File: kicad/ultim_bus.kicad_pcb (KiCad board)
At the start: 2 copper layers, 16 parts, among them P1 CONN_1, P10 CONN_1, P11 CONN_1, P12 CONN_1, P2 CONN_1, P3 CONN_1, P4 CONN_1, P5 CONN_1, P6 CONN_1, P7 CONN_1, P8 CONN_1, P9 CONN_1

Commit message: UlTiM8x8 board layout complete, Gerbers ready for fab
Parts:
- removed G***: LOGO, ultim8x8_libs:logo_ultim8x8_small
- removed G***: LOGO, ultim8x8_libs:logo_wyo_butterfly_small
- removed G***: LOGO, ultim8x8_libs:logo_MLlabs_small
- removed L101: OSHW, ultim8x8_libs:OSHW_6mm
- added L1: OSHW, ultim8x8_libs:OSHW_6mm, F.Cu at (210.8, 38.1)
- added L10: Maniacal, ultim8x8_libs:logo_MLlabs_small, F.Cu at (165.1, 55.9)
- added L11: Maniacal, ultim8x8_libs:logo_MLlabs_small, F.Cu at (149.9, 68.6)
- added L12: Maniacal, ultim8x8_libs:logo_MLlabs_small, F.Cu at (149.9, 91.4)
- added L13: ULTiM, ultim8x8_libs:logo_ultim8x8_small, F.Cu at (58.4, 38.1)
- added L14: ULTiM, ultim8x8_libs:logo_ultim8x8_small, F.Cu at (73.7, 55.9)
- added L15: ULTiM, ultim8x8_libs:logo_ultim8x8_small, F.Cu at (58.4, 69.2)
- added L16: ULTiM, ultim8x8_libs:logo_ultim8x8_small, F.Cu at (58.4, 91.4)
- added L2: OSHW, ultim8x8_libs:OSHW_6mm, F.Cu at (196.8, 55.2)
- added L3: OSHW, ultim8x8_libs:OSHW_6mm, F.Cu at (210.8, 68.6)
- added L4: OSHW, ultim8x8_libs:OSHW_6mm, F.Cu at (210.8, 91.4)
- added L5: WyoLum, ultim8x8_libs:logo_wyo_butterfly_small, F.Cu at (119.4, 38.1)
- added L6: WyoLum, ultim8x8_libs:logo_wyo_butterfly_small, F.Cu at (104.8, 57.1)
- added L7: WyoLum, ultim8x8_libs:logo_wyo_butterfly_small, F.Cu at (119.4, 68.6)
- added L8: WyoLum, ultim8x8_libs:logo_wyo_butterfly_small, F.Cu at (104.8, 92.1)
- added L9: Maniacal, ultim8x8_libs:logo_MLlabs_small, F.Cu at (149.9, 38.1)
- added P13: CONN_1, ultim8x8_libs:Screw, F.Cu at (50.8, 50.8)
- added P14: CONN_1, ultim8x8_libs:Screw, F.Cu at (66.0, 50.8)
- added P15: CONN_1, ultim8x8_libs:Screw, F.Cu at (81.3, 50.8)
- added P16: CONN_1, ultim8x8_libs:Screw, F.Cu at (96.5, 50.8)
- added P17: CONN_1, ultim8x8_libs:Screw, F.Cu at (111.8, 50.8)
- added P18: CONN_1, ultim8x8_libs:Screw, F.Cu at (127.0, 50.8)
- added P19: CONN_1, ultim8x8_libs:Screw, F.Cu at (142.2, 50.8)
- added P20: CONN_1, ultim8x8_libs:Screw, F.Cu at (157.5, 50.8)
- added P21: CONN_1, ultim8x8_libs:Screw, F.Cu at (172.7, 50.8)
- added P22: CONN_1, ultim8x8_libs:Screw, F.Cu at (188.0, 50.8)
- added P23: CONN_1, ultim8x8_libs:Screw, F.Cu at (203.2, 50.8)
- added P24: CONN_1, ultim8x8_libs:Screw, F.Cu at (218.4, 50.8)
- added P25: CONN_1, ultim8x8_libs:Screw, F.Cu at (58.4, 55.9)
- added P26: CONN_1, ultim8x8_libs:Screw, F.Cu at (88.9, 55.9)
- added P27: CONN_1, ultim8x8_libs:Screw, F.Cu at (119.4, 55.9)
- added P28: CONN_1, ultim8x8_libs:Screw, F.Cu at (149.9, 55.9)
- added P29: CONN_1, ultim8x8_libs:Screw, F.Cu at (180.3, 55.9)
- added P30: CONN_1, ultim8x8_libs:Screw, F.Cu at (210.8, 55.9)
- added P31: CONN_1, ultim8x8_libs:Screw, F.Cu at (50.8, 68.6)
- added P32: CONN_1, ultim8x8_libs:Screw, F.Cu at (66.0, 68.6)
- added P33: CONN_1, ultim8x8_libs:Screw, F.Cu at (81.3, 68.6)
- added P34: CONN_1, ultim8x8_libs:Screw, F.Cu at (96.5, 68.6)
- added P35: CONN_1, ultim8x8_libs:Screw, F.Cu at (111.8, 68.6)
- added P36: CONN_1, ultim8x8_libs:Screw, F.Cu at (127.0, 68.6)
- added P37: CONN_1, ultim8x8_libs:Screw, F.Cu at (142.2, 68.6)
- added P38: CONN_1, ultim8x8_libs:Screw, F.Cu at (157.5, 68.6)
- added P39: CONN_1, ultim8x8_libs:Screw, F.Cu at (172.7, 68.6)
- added P40: CONN_1, ultim8x8_libs:Screw, F.Cu at (188.0, 68.6)
- added P41: CONN_1, ultim8x8_libs:Screw, F.Cu at (203.2, 68.6)
- added P42: CONN_1, ultim8x8_libs:Screw, F.Cu at (218.4, 68.6)
- added P43: CONN_1, ultim8x8_libs:Screw, F.Cu at (50.8, 78.7)
- added P44: CONN_1, ultim8x8_libs:Screw, F.Cu at (81.3, 78.7)
- added P45: CONN_1, ultim8x8_libs:Screw, F.Cu at (111.8, 78.7)
- added P46: CONN_1, ultim8x8_libs:Screw, F.Cu at (142.2, 78.7)
- added P47: CONN_1, ultim8x8_libs:Screw, F.Cu at (172.7, 78.7)
- added P48: CONN_1, ultim8x8_libs:Screw, F.Cu at (203.2, 78.7)
- added P49: CONN_1, ultim8x8_libs:Screw, F.Cu at (50.8, 91.4)
- added P50: CONN_1, ultim8x8_libs:Screw, F.Cu at (66.0, 91.4)
- added P51: CONN_1, ultim8x8_libs:Screw, F.Cu at (81.3, 91.4)
- added P52: CONN_1, ultim8x8_libs:Screw, F.Cu at (96.5, 91.4)
- added P53: CONN_1, ultim8x8_libs:Screw, F.Cu at (111.8, 91.4)
- added P54: CONN_1, ultim8x8_libs:Screw, F.Cu at (127.0, 91.4)
- added P55: CONN_1, ultim8x8_libs:Screw, F.Cu at (142.2, 91.4)
- added P56: CONN_1, ultim8x8_libs:Screw, F.Cu at (157.5, 91.4)
- added P57: CONN_1, ultim8x8_libs:Screw, F.Cu at (172.7, 91.4)
- added P58: CONN_1, ultim8x8_libs:Screw, F.Cu at (188.0, 91.4)
- added P59: CONN_1, ultim8x8_libs:Screw, F.Cu at (203.2, 91.4)
- added P60: CONN_1, ultim8x8_libs:Screw, F.Cu at (218.4, 91.4)
- added P61: CONN_1, ultim8x8_libs:Screw, F.Cu at (66.0, 81.3)
- added P62: CONN_1, ultim8x8_libs:Screw, F.Cu at (96.5, 81.3)
- added P63: CONN_1, ultim8x8_libs:Screw, F.Cu at (127.0, 81.3)
- added P64: CONN_1, ultim8x8_libs:Screw, F.Cu at (157.5, 81.3)
- added P65: CONN_1, ultim8x8_libs:Screw, F.Cu at (188.0, 81.3)
- added P66: CONN_1, ultim8x8_libs:Screw, F.Cu at (218.4, 81.3)
- added mouse-bite-2.54mm-slot: VAL**, ultim8x8_libs:mouse-bite-2.54mm-slot, F.Cu at (96.5, 44.5)
- added mouse-bite-2.54mm-slot: VAL**, ultim8x8_libs:mouse-bite-2.54mm-slot, F.Cu at (127.0, 76.2)
- added mouse-bite-2.54mm-slot: VAL**, ultim8x8_libs:mouse-bite-2.54mm-slot, F.Cu at (96.5, 76.2)
- added mouse-bite-2.54mm-slot: VAL**, ultim8x8_libs:mouse-bite-2.54mm-slot, F.Cu at (66.0, 76.2)
- added mouse-bite-2.54mm-slot: VAL**, ultim8x8_libs:mouse-bite-2.54mm-slot, F.Cu at (157.5, 44.5)
- added mouse-bite-2.54mm-slot: VAL**, ultim8x8_libs:mouse-bite-2.54mm-slot, F.Cu at (218.4, 44.5)
- added mouse-bite-2.54mm-slot: VAL**, ultim8x8_libs:mouse-bite-2.54mm-slot, F.Cu at (188.0, 62.2)
- added mouse-bite-2.54mm-slot: VAL**, ultim8x8_libs:mouse-bite-2.54mm-slot, F.Cu at (66.0, 62.2)
- added mouse-bite-2.54mm-slot: VAL**, ultim8x8_libs:mouse-bite-2.54mm-slot, F.Cu at (127.0, 62.2)
- added mouse-bite-2.54mm-slot: VAL**, ultim8x8_libs:mouse-bite-2.54mm-slot, F.Cu at (218.4, 76.2)
- added mouse-bite-2.54mm-slot: VAL**, ultim8x8_libs:mouse-bite-2.54mm-slot, F.Cu at (188.0, 76.2)
- added mouse-bite-2.54mm-slot: VAL**, ultim8x8_libs:mouse-bite-2.54mm-slot, F.Cu at (157.5, 76.2)
- moved P1 12.7 mm to (50.8, 38.1)
- moved P10 12.7 mm to (157.5, 38.1)
- moved P11 12.7 mm to (188.0, 38.1)
- moved P12 12.7 mm to (218.4, 38.1)
- moved P2 12.7 mm to (81.3, 38.1)
- moved P3 12.7 mm to (111.8, 38.1)
- moved P4 12.7 mm to (142.2, 38.1)
- moved P5 12.7 mm to (172.7, 38.1)
- moved P6 12.7 mm to (203.2, 38.1)
- moved P7 12.7 mm to (66.0, 38.1)
- moved P8 12.7 mm to (96.5, 38.1)
- moved P9 12.7 mm to (127.0, 38.1)
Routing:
- net Net-(P13-Pad1): track 0.00 -> 167.6 mm
- net Net-(P49-Pad1): track 0.00 -> 167.6 mm
- net Net-(P31-Pad1): track 0.00 -> 167.6 mm
- net Net-(P1-Pad1): track 0.00 -> 167.6 mm
- added copper zone on B.Cu, net Net-(P1-Pad1)
- added copper zone on F.Cu, net Net-(P1-Pad1)
- added copper zone on B.Cu, net Net-(P13-Pad1)
- added copper zone on F.Cu, net Net-(P13-Pad1)
- added copper zone on B.Cu, net Net-(P31-Pad1)
- added copper zone on F.Cu, net Net-(P31-Pad1)
- added copper zone on B.Cu, net Net-(P49-Pad1)
- added copper zone on F.Cu, net Net-(P49-Pad1)
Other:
- board outline added: 182.9 x 63.5 mm
- board text added: "5V"
- board text added: "GND"

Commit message: UlTiM_bus layout, gerber complete. Bus accessory for ULTiM8x8
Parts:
- removed mouse-bite-2.54mm-slot (x12): VAL**, ultim8x8_libs:mouse-bite-2.54mm-slot
- added M1: MouseBite, ultim8x8_libs:mouse-bite-2.54mm-slot, F.Cu at (35.6, 44.5)
- added M10: MouseBite, ultim8x8_libs:mouse-bite-2.54mm-slot, F.Cu at (66.0, 76.2)
- added M11: MouseBite, ultim8x8_libs:mouse-bite-2.54mm-slot, F.Cu at (96.5, 76.2)
- added M12: MouseBite, ultim8x8_libs:mouse-bite-2.54mm-slot, F.Cu at (127.0, 76.2)
- added M13: MouseBite, ultim8x8_libs:mouse-bite-2.54mm-slot, F.Cu at (157.5, 76.2)
- added M14: MouseBite, ultim8x8_libs:mouse-bite-2.54mm-slot, F.Cu at (188.0, 76.2)
- added M15: MouseBite, ultim8x8_libs:mouse-bite-2.54mm-slot, F.Cu at (218.4, 76.2)
- added M2: MouseBite, ultim8x8_libs:mouse-bite-2.54mm-slot, F.Cu at (96.5, 44.5)
- added M3: MouseBite, ultim8x8_libs:mouse-bite-2.54mm-slot, F.Cu at (157.5, 44.5)
- added M4: MouseBite, ultim8x8_libs:mouse-bite-2.54mm-slot, F.Cu at (218.4, 44.5)
- added M5: MouseBite, ultim8x8_libs:mouse-bite-2.54mm-slot, F.Cu at (35.6, 62.2)
- added M6: MouseBite, ultim8x8_libs:mouse-bite-2.54mm-slot, F.Cu at (96.5, 62.2)
- added M7: MouseBite, ultim8x8_libs:mouse-bite-2.54mm-slot, F.Cu at (157.5, 62.2)
- added M8: MouseBite, ultim8x8_libs:mouse-bite-2.54mm-slot, F.Cu at (218.4, 62.2)
- added M9: MouseBite, ultim8x8_libs:mouse-bite-2.54mm-slot, F.Cu at (35.6, 76.2)
- added P67: CONN_1, ultim8x8_libs:Screw, F.Cu at (35.6, 38.1)
- added P68: CONN_1, ultim8x8_libs:Screw, F.Cu at (35.6, 50.8)
- added P69: CONN_1, ultim8x8_libs:Screw, F.Cu at (35.6, 68.6)
- added P70: CONN_1, ultim8x8_libs:Screw, F.Cu at (35.6, 91.4)
- added P71: CONN_1, ultim8x8_libs:Screw, F.Cu at (35.6, 81.3)
- added REF**11: via_0.8, ultim8x8_libs:via_0.8, F.Cu at (176.5, 33.0)
- added REF**11: via_0.8, ultim8x8_libs:via_0.8, F.Cu at (176.5, 34.3)
- added REF**111: via_0.8, ultim8x8_libs:via_0.8, F.Cu at (54.6, 33.0)
- added REF**1111: via_0.8, ultim8x8_libs:via_0.8, F.Cu at (115.6, 33.0)
- added REF**1111: via_0.8, ultim8x8_libs:via_0.8, F.Cu at (176.5, 45.7)
- added REF**11110: via_0.8, ultim8x8_libs:via_0.8, F.Cu at (176.5, 57.1)
- added REF**11111: via_0.8, ultim8x8_libs:via_0.8, F.Cu at (54.6, 45.7)
- added REF**11111: via_0.8, ultim8x8_libs:via_0.8, F.Cu at (115.6, 45.7)
- added REF**11111: via_0.8, ultim8x8_libs:via_0.8, F.Cu at (176.5, 58.4)
- added REF**111110: via_0.8, ultim8x8_libs:via_0.8, F.Cu at (54.6, 57.1)
- added REF**111110: via_0.8, ultim8x8_libs:via_0.8, F.Cu at (115.6, 57.1)
- added REF**111111: via_0.8, ultim8x8_libs:via_0.8, F.Cu at (54.6, 58.4)
- added REF**111111: via_0.8, ultim8x8_libs:via_0.8, F.Cu at (115.6, 58.4)
- added REF**111111: via_0.8, ultim8x8_libs:via_0.8, F.Cu at (176.5, 63.5)
- added REF**1111110: via_0.8, ultim8x8_libs:via_0.8, F.Cu at (176.5, 74.9)
- added REF**1111111: via_0.8, ultim8x8_libs:via_0.8, F.Cu at (54.6, 63.5)
- added REF**1111111: via_0.8, ultim8x8_libs:via_0.8, F.Cu at (115.6, 63.5)
- added REF**1111111: via_0.8, ultim8x8_libs:via_0.8, F.Cu at (176.5, 76.2)
- added REF**11111110: via_0.8, ultim8x8_libs:via_0.8, F.Cu at (54.6, 74.9)
- added REF**11111110: via_0.8, ultim8x8_libs:via_0.8, F.Cu at (115.6, 74.9)
- added REF**11111111: via_0.8, ultim8x8_libs:via_0.8, F.Cu at (54.6, 76.2)
- added REF**11111111: via_0.8, ultim8x8_libs:via_0.8, F.Cu at (115.6, 76.2)
- added REF**11111111: via_0.8, ultim8x8_libs:via_0.8, F.Cu at (176.5, 85.1)
- added REF**111111110: via_0.8, ultim8x8_libs:via_0.8, F.Cu at (176.5, 96.5)
- added REF**111111111: via_0.8, ultim8x8_libs:via_0.8, F.Cu at (54.6, 85.1)
- added REF**111111111: via_0.8, ultim8x8_libs:via_0.8, F.Cu at (115.6, 85.1)
- added REF**1111111110: via_0.8, ultim8x8_libs:via_0.8, F.Cu at (54.6, 96.5)
- added REF**1111111110: via_0.8, ultim8x8_libs:via_0.8, F.Cu at (115.6, 96.5)
- added REF**111111112: via_0.8, ultim8x8_libs:via_0.8, F.Cu at (54.6, 86.4)
- added REF**111111112: via_0.8, ultim8x8_libs:via_0.8, F.Cu at (115.6, 86.4)
- added REF**111111113: via_0.8, ultim8x8_libs:via_0.8, F.Cu at (54.6, 87.6)
- added REF**111111113: via_0.8, ultim8x8_libs:via_0.8, F.Cu at (115.6, 87.6)
- added REF**111111114: via_0.8, ultim8x8_libs:via_0.8, F.Cu at (54.6, 88.9)
- added REF**111111114: via_0.8, ultim8x8_libs:via_0.8, F.Cu at (115.6, 88.9)
- added REF**111111115: via_0.8, ultim8x8_libs:via_0.8, F.Cu at (54.6, 90.2)
- added REF**111111115: via_0.8, ultim8x8_libs:via_0.8, F.Cu at (115.6, 90.2)
- added REF**111111116: via_0.8, ultim8x8_libs:via_0.8, F.Cu at (54.6, 91.4)
- added REF**111111116: via_0.8, ultim8x8_libs:via_0.8, F.Cu at (115.6, 91.4)
- added REF**111111117: via_0.8, ultim8x8_libs:via_0.8, F.Cu at (54.6, 92.7)
- added REF**111111117: via_0.8, ultim8x8_libs:via_0.8, F.Cu at (115.6, 92.7)
- added REF**111111118: via_0.8, ultim8x8_libs:via_0.8, F.Cu at (54.6, 94.0)
- added REF**111111118: via_0.8, ultim8x8_libs:via_0.8, F.Cu at (115.6, 94.0)
- added REF**111111119: via_0.8, ultim8x8_libs:via_0.8, F.Cu at (54.6, 95.2)
- added REF**111111119: via_0.8, ultim8x8_libs:via_0.8, F.Cu at (115.6, 95.2)
- added REF**11111112: via_0.8, ultim8x8_libs:via_0.8, F.Cu at (54.6, 77.5)
- added REF**11111112: via_0.8, ultim8x8_libs:via_0.8, F.Cu at (115.6, 77.5)
- added REF**11111112: via_0.8, ultim8x8_libs:via_0.8, F.Cu at (176.5, 86.4)
- added REF**11111113: via_0.8, ultim8x8_libs:via_0.8, F.Cu at (54.6, 78.7)
- added REF**11111113: via_0.8, ultim8x8_libs:via_0.8, F.Cu at (115.6, 78.7)
- added REF**11111113: via_0.8, ultim8x8_libs:via_0.8, F.Cu at (176.5, 87.6)
- added REF**11111114: via_0.8, ultim8x8_libs:via_0.8, F.Cu at (54.6, 80.0)
- added REF**11111114: via_0.8, ultim8x8_libs:via_0.8, F.Cu at (115.6, 80.0)
- added REF**11111114: via_0.8, ultim8x8_libs:via_0.8, F.Cu at (176.5, 88.9)
- added REF**11111115: via_0.8, ultim8x8_libs:via_0.8, F.Cu at (54.6, 81.3)
- added REF**11111115: via_0.8, ultim8x8_libs:via_0.8, F.Cu at (115.6, 81.3)
- added REF**11111115: via_0.8, ultim8x8_libs:via_0.8, F.Cu at (176.5, 90.2)
- added REF**11111116: via_0.8, ultim8x8_libs:via_0.8, F.Cu at (54.6, 82.5)
- added REF**11111116: via_0.8, ultim8x8_libs:via_0.8, F.Cu at (115.6, 82.5)
- added REF**11111116: via_0.8, ultim8x8_libs:via_0.8, F.Cu at (176.5, 91.4)
- added REF**11111117: via_0.8, ultim8x8_libs:via_0.8, F.Cu at (176.5, 92.7)
- added REF**11111118: via_0.8, ultim8x8_libs:via_0.8, F.Cu at (176.5, 94.0)
- added REF**11111119: via_0.8, ultim8x8_libs:via_0.8, F.Cu at (176.5, 95.2)
- added REF**1111112: via_0.8, ultim8x8_libs:via_0.8, F.Cu at (54.6, 64.8)
- added REF**1111112: via_0.8, ultim8x8_libs:via_0.8, F.Cu at (115.6, 64.8)
- added REF**1111112: via_0.8, ultim8x8_libs:via_0.8, F.Cu at (176.5, 77.5)
- added REF**1111113: via_0.8, ultim8x8_libs:via_0.8, F.Cu at (54.6, 66.0)
- added REF**1111113: via_0.8, ultim8x8_libs:via_0.8, F.Cu at (115.6, 66.0)
- added REF**1111113: via_0.8, ultim8x8_libs:via_0.8, F.Cu at (176.5, 78.7)
- added REF**1111114: via_0.8, ultim8x8_libs:via_0.8, F.Cu at (54.6, 67.3)
- added REF**1111114: via_0.8, ultim8x8_libs:via_0.8, F.Cu at (115.6, 67.3)
- added REF**1111114: via_0.8, ultim8x8_libs:via_0.8, F.Cu at (176.5, 80.0)
- added REF**1111115: via_0.8, ultim8x8_libs:via_0.8, F.Cu at (54.6, 68.6)
- added REF**1111115: via_0.8, ultim8x8_libs:via_0.8, F.Cu at (115.6, 68.6)
- added REF**1111115: via_0.8, ultim8x8_libs:via_0.8, F.Cu at (176.5, 81.3)
- added REF**1111116: via_0.8, ultim8x8_libs:via_0.8, F.Cu at (54.6, 69.8)
- added REF**1111116: via_0.8, ultim8x8_libs:via_0.8, F.Cu at (115.6, 69.8)
- added REF**1111116: via_0.8, ultim8x8_libs:via_0.8, F.Cu at (176.5, 82.5)
- added REF**1111117: via_0.8, ultim8x8_libs:via_0.8, F.Cu at (54.6, 71.1)
- added REF**1111117: via_0.8, ultim8x8_libs:via_0.8, F.Cu at (115.6, 71.1)
- added REF**1111118: via_0.8, ultim8x8_libs:via_0.8, F.Cu at (54.6, 72.4)
- added REF**1111118: via_0.8, ultim8x8_libs:via_0.8, F.Cu at (115.6, 72.4)
- added REF**1111119: via_0.8, ultim8x8_libs:via_0.8, F.Cu at (54.6, 73.7)
- added REF**1111119: via_0.8, ultim8x8_libs:via_0.8, F.Cu at (115.6, 73.7)
- added REF**111112: via_0.8, ultim8x8_libs:via_0.8, F.Cu at (54.6, 59.7)
- added REF**111112: via_0.8, ultim8x8_libs:via_0.8, F.Cu at (115.6, 59.7)
- added REF**111112: via_0.8, ultim8x8_libs:via_0.8, F.Cu at (176.5, 64.8)
- added REF**111113: via_0.8, ultim8x8_libs:via_0.8, F.Cu at (54.6, 61.0)
- added REF**111113: via_0.8, ultim8x8_libs:via_0.8, F.Cu at (115.6, 61.0)
- added REF**111113: via_0.8, ultim8x8_libs:via_0.8, F.Cu at (176.5, 66.0)
- added REF**111114: via_0.8, ultim8x8_libs:via_0.8, F.Cu at (176.5, 67.3)
- added REF**111115: via_0.8, ultim8x8_libs:via_0.8, F.Cu at (176.5, 68.6)
- added REF**111116: via_0.8, ultim8x8_libs:via_0.8, F.Cu at (176.5, 69.8)
- added REF**111117: via_0.8, ultim8x8_libs:via_0.8, F.Cu at (176.5, 71.1)
- added REF**111118: via_0.8, ultim8x8_libs:via_0.8, F.Cu at (176.5, 72.4)
- added REF**111119: via_0.8, ultim8x8_libs:via_0.8, F.Cu at (176.5, 73.7)
- added REF**11112: via_0.8, ultim8x8_libs:via_0.8, F.Cu at (54.6, 47.0)
- added REF**11112: via_0.8, ultim8x8_libs:via_0.8, F.Cu at (115.6, 47.0)
- added REF**11112: via_0.8, ultim8x8_libs:via_0.8, F.Cu at (176.5, 59.7)
- added REF**11113: via_0.8, ultim8x8_libs:via_0.8, F.Cu at (54.6, 48.3)
- added REF**11113: via_0.8, ultim8x8_libs:via_0.8, F.Cu at (115.6, 48.3)
- added REF**11113: via_0.8, ultim8x8_libs:via_0.8, F.Cu at (176.5, 61.0)
- added REF**11114: via_0.8, ultim8x8_libs:via_0.8, F.Cu at (54.6, 49.5)
- added REF**11114: via_0.8, ultim8x8_libs:via_0.8, F.Cu at (115.6, 49.5)
- added REF**11115: via_0.8, ultim8x8_libs:via_0.8, F.Cu at (54.6, 50.8)
- added REF**11115: via_0.8, ultim8x8_libs:via_0.8, F.Cu at (115.6, 50.8)
- added REF**11116: via_0.8, ultim8x8_libs:via_0.8, F.Cu at (54.6, 52.1)
- added REF**11116: via_0.8, ultim8x8_libs:via_0.8, F.Cu at (115.6, 52.1)
- added REF**11117: via_0.8, ultim8x8_libs:via_0.8, F.Cu at (54.6, 53.3)
- added REF**11117: via_0.8, ultim8x8_libs:via_0.8, F.Cu at (115.6, 53.3)
- added REF**11118: via_0.8, ultim8x8_libs:via_0.8, F.Cu at (54.6, 54.6)
- added REF**11118: via_0.8, ultim8x8_libs:via_0.8, F.Cu at (115.6, 54.6)
- added REF**11119: via_0.8, ultim8x8_libs:via_0.8, F.Cu at (54.6, 55.9)
- added REF**11119: via_0.8, ultim8x8_libs:via_0.8, F.Cu at (115.6, 55.9)
- added REF**1112: via_0.8, ultim8x8_libs:via_0.8, F.Cu at (115.6, 34.3)
- added REF**1112: via_0.8, ultim8x8_libs:via_0.8, F.Cu at (176.5, 47.0)
- added REF**1113: via_0.8, ultim8x8_libs:via_0.8, F.Cu at (115.6, 35.6)
- added REF**1113: via_0.8, ultim8x8_libs:via_0.8, F.Cu at (176.5, 48.3)
- added REF**1114: via_0.8, ultim8x8_libs:via_0.8, F.Cu at (115.6, 36.8)
- added REF**1114: via_0.8, ultim8x8_libs:via_0.8, F.Cu at (176.5, 49.5)
- added REF**1115: via_0.8, ultim8x8_libs:via_0.8, F.Cu at (115.6, 38.1)
- added REF**1115: via_0.8, ultim8x8_libs:via_0.8, F.Cu at (176.5, 50.8)
- added REF**1116: via_0.8, ultim8x8_libs:via_0.8, F.Cu at (115.6, 39.4)
- added REF**1116: via_0.8, ultim8x8_libs:via_0.8, F.Cu at (176.5, 52.1)
- added REF**1117: via_0.8, ultim8x8_libs:via_0.8, F.Cu at (115.6, 40.6)
- added REF**1117: via_0.8, ultim8x8_libs:via_0.8, F.Cu at (176.5, 53.3)
- added REF**1118: via_0.8, ultim8x8_libs:via_0.8, F.Cu at (115.6, 41.9)
- added REF**1118: via_0.8, ultim8x8_libs:via_0.8, F.Cu at (176.5, 54.6)
- added REF**1119: via_0.8, ultim8x8_libs:via_0.8, F.Cu at (115.6, 43.2)
- added REF**1119: via_0.8, ultim8x8_libs:via_0.8, F.Cu at (176.5, 55.9)
- added REF**112: via_0.8, ultim8x8_libs:via_0.8, F.Cu at (54.6, 34.3)
- added REF**113: via_0.8, ultim8x8_libs:via_0.8, F.Cu at (54.6, 35.6)
- added REF**114: via_0.8, ultim8x8_libs:via_0.8, F.Cu at (54.6, 36.8)
- added REF**115: via_0.8, ultim8x8_libs:via_0.8, F.Cu at (54.6, 38.1)
- added REF**116: via_0.8, ultim8x8_libs:via_0.8, F.Cu at (54.6, 39.4)
- added REF**117: via_0.8, ultim8x8_libs:via_0.8, F.Cu at (54.6, 40.6)
- added REF**118: via_0.8, ultim8x8_libs:via_0.8, F.Cu at (54.6, 41.9)
- added REF**119: via_0.8, ultim8x8_libs:via_0.8, F.Cu at (54.6, 43.2)
- added REF**12: via_0.8, ultim8x8_libs:via_0.8, F.Cu at (176.5, 35.6)
- added REF**13: via_0.8, ultim8x8_libs:via_0.8, F.Cu at (176.5, 36.8)
- added REF**14: via_0.8, ultim8x8_libs:via_0.8, F.Cu at (176.5, 38.1)
- added REF**15: via_0.8, ultim8x8_libs:via_0.8, F.Cu at (176.5, 39.4)
- added REF**16: via_0.8, ultim8x8_libs:via_0.8, F.Cu at (176.5, 40.6)
- added REF**17: via_0.8, ultim8x8_libs:via_0.8, F.Cu at (176.5, 43.2)
- added REF**17: via_0.8, ultim8x8_libs:via_0.8, F.Cu at (176.5, 41.9)
- moved L1 45.7 mm to (165.1, 38.1)
- moved L3 45.7 mm to (165.1, 68.6)
- moved L4 45.7 mm to (165.1, 91.4)
- moved L2 32.1 mm to (165.1, 50.8)
- moved L10 30.9 mm to (134.6, 50.8)
- moved L15 15.3 mm to (73.7, 68.6)
- moved L11 15.2 mm to (134.6, 68.6)
- moved L12 15.2 mm to (134.6, 91.4)
- moved L9 15.2 mm to (134.6, 38.1)
- moved L13 15.2 mm to (73.7, 38.1)
- moved L16 15.2 mm to (73.7, 91.4)
- moved L5 15.2 mm to (104.1, 38.1)
- moved L7 15.2 mm to (104.1, 68.6)
- moved L6 6.38 mm to (104.1, 50.8)
- moved L14 5.08 mm to (73.7, 50.8)
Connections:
- net Net-(P1-Pad1) renamed /ROW1
- net Net-(P13-Pad1) renamed /ROW2
- net Net-(P31-Pad1) renamed /ROW3
- net Net-(P49-Pad1) renamed /ROW4
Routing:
- net /ROW3: track 167.6 -> 213.4 mm
- net /ROW4: track 167.6 -> 190.5 mm
- net /ROW2: track 167.6 -> 182.9 mm
- net /ROW1: track 167.6 -> 175.3 mm
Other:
- board size 182.9 x 63.5 mm -> 198.1 x 63.5 mm

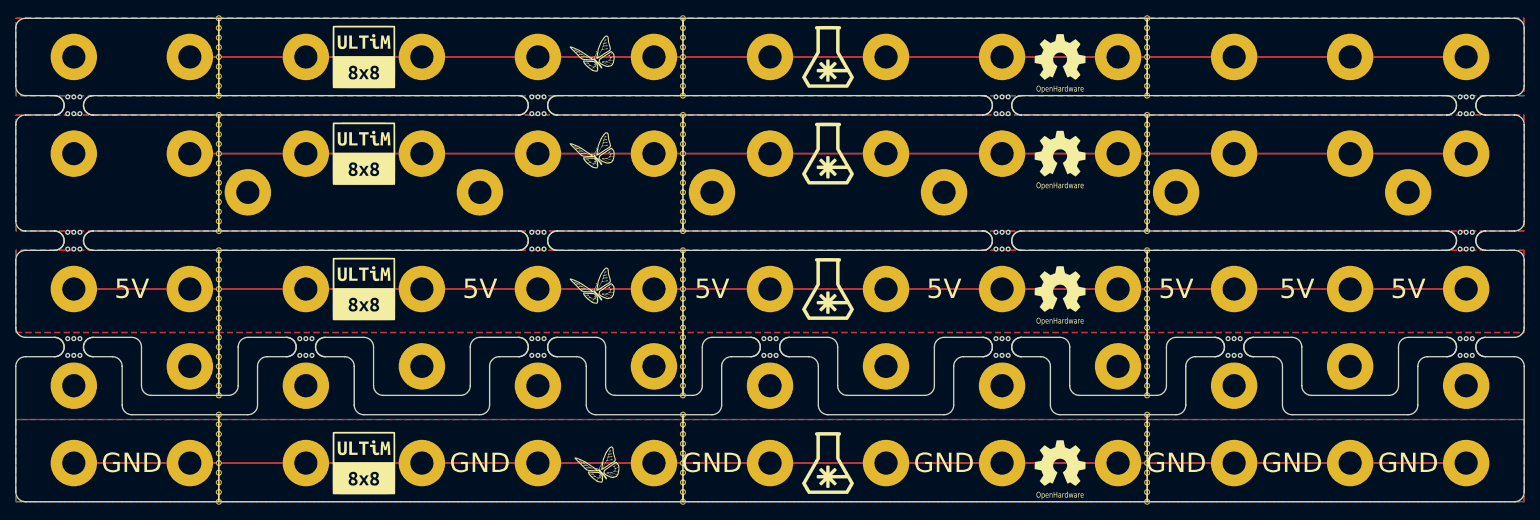
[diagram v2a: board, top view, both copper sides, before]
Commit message: UlTiM_bus layout, gerber complete. Bus accessory for ULTiM8x8
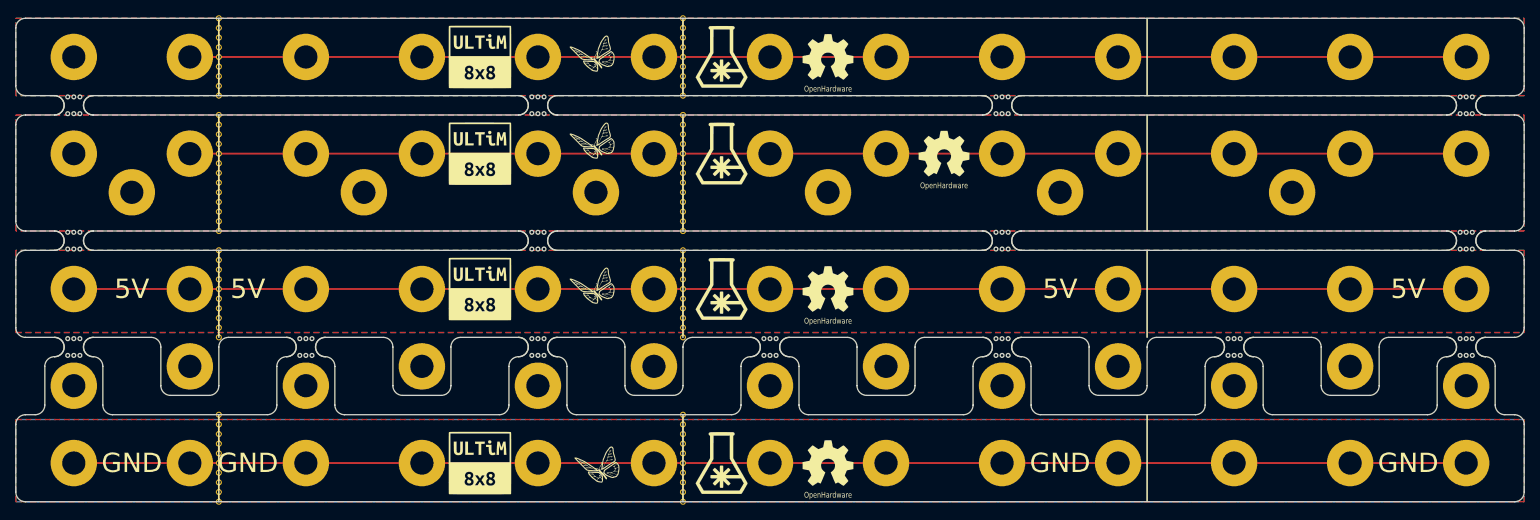
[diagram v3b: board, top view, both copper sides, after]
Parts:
- removed REF**11 (x2), REF**11110, REF**1111110, REF**11111111 (x3), REF**111111110, REF**11111112 (x3), REF**11111113 (x3), REF**11111114 (x3), REF**11111115 (x3), REF**11111116 (x3), REF**11111117, REF**11111118, REF**11111119, REF**111114, REF**111115, REF**111116, REF**111117, REF**111118, REF**111119, REF**12, REF**13, REF**14, REF**15, REF**16, REF**17 (x2): via_0.8, ultim8x8_libs:via_0.8
- removed the REF**1111 at (176.5, 45.7)
- removed the REF**11111 at (176.5, 58.4)
- removed the REF**111111 at (176.5, 63.5)
- removed the REF**1111111 at (176.5, 76.2)
- removed the REF**1111112 at (176.5, 77.5)
- removed the REF**1111113 at (176.5, 78.7)
- removed the REF**1111114 at (176.5, 80.0)
- removed the REF**1111115 at (176.5, 81.3)
- removed the REF**1111116 at (176.5, 82.5)
- removed the REF**111112 at (176.5, 64.8)
- removed the REF**111113 at (176.5, 66.0)
- removed the REF**11112 at (176.5, 59.7)
- removed the REF**11113 at (176.5, 61.0)
- removed the REF**1112 at (176.5, 47.0)
- removed the REF**1113 at (176.5, 48.3)
- removed the REF**1114 at (176.5, 49.5)
- removed the REF**1115 at (176.5, 50.8)
- removed the REF**1116 at (176.5, 52.1)
- removed the REF**1117 at (176.5, 53.3)
- removed the REF**1118 at (176.5, 54.6)
- removed the REF**1119 at (176.5, 55.9)
- moved L1 30.5 mm to (134.6, 38.1)
- moved L3 30.5 mm to (134.6, 68.6)
- moved L4 30.5 mm to (134.6, 91.4)
- moved L13 15.2 mm to (88.9, 38.1)
- moved L14 15.2 mm to (88.9, 50.8)
- moved L15 15.2 mm to (88.9, 68.6)
- moved L16 15.2 mm to (88.9, 91.4)
- moved P26 15.2 mm to (73.7, 55.9)
- moved P28 15.2 mm to (134.6, 55.9)
- moved P29 15.2 mm to (165.1, 55.9)
- moved P25 15.2 mm to (43.2, 55.9)
- moved P27 15.2 mm to (104.1, 55.9)
- moved L2 15.2 mm to (149.9, 50.8)
- moved P30 15.2 mm to (195.6, 55.9)
- moved L10 14.0 mm to (120.7, 50.8)
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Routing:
- net /ROW4: track 190.5 -> 206.4 mm
- net /ROW2: track 182.9 -> 198.8 mm
- net /ROW1: track 175.3 -> 188.0 mm
- net /ROW3: track 213.4 -> 205.7 mm
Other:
- outline, holes or cut-outs redrawn
